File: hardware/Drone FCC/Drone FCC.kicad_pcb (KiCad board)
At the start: 4 copper layers, 60 x 100 mm, 160 parts, among them J1 UARTs externo x 3, J1001 SPI externo, J1003 I2C externo x2, J1005 5V y 3V3 x 2, J201 Mag Dupont, J202 Mag DF13, J203 GPS Dupont, J204 GPS M8N - DF13, J301 ESC 1, J302 ESC 2, J303 ESC 3, J304 ESC 4, J305 ESC 5, J306 ESC 6, J307 ESC 7, J308 ESC 8, J309 SERVO 1, J310 SERVO 2, J311 SERVO 3, J312 SERVO 4, J313 Power Servo, J401 DSM Spektrum JST, J402 PPM Dupont, J501 Micro USB - B, J601 SWD Debug Connector, J701 DM3AT-SF-PEJM5, J801 CAN 1 Connector 1, J803 CAN 2 Connector 1, J901 PM02 PixHawk, Q1101 2N7002, Q1102 2N7002, Q1103 2N7002, Q1104 2N7002, Q1105 2N7002, Q1106 2N7002, Q1107 2N7002, Q1108 2N7002, SW101 SW RESET, SW1101 SW Proposito General, SW1102 SW Proposito General, U101 STM32F746ZGTx, U201 ICM-42688-V, U202 HLGA_10L_STM, U501 USBLC6-2SC6, U801 SN65HVD230, U802 SN65HVD230, U901 ZLDO1117QG33TA, Y101 12MHz, Y102 32.768kHz

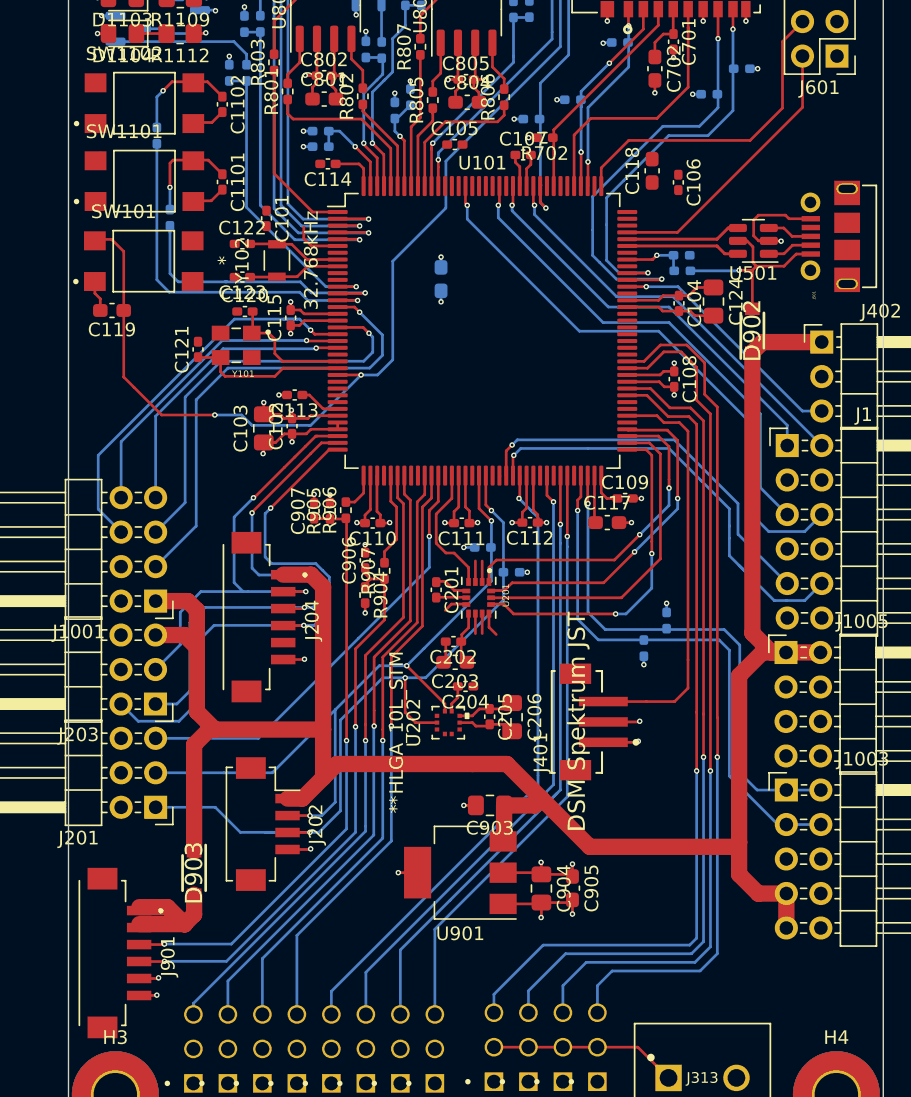
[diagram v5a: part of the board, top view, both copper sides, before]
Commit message: LDO layout on PCB
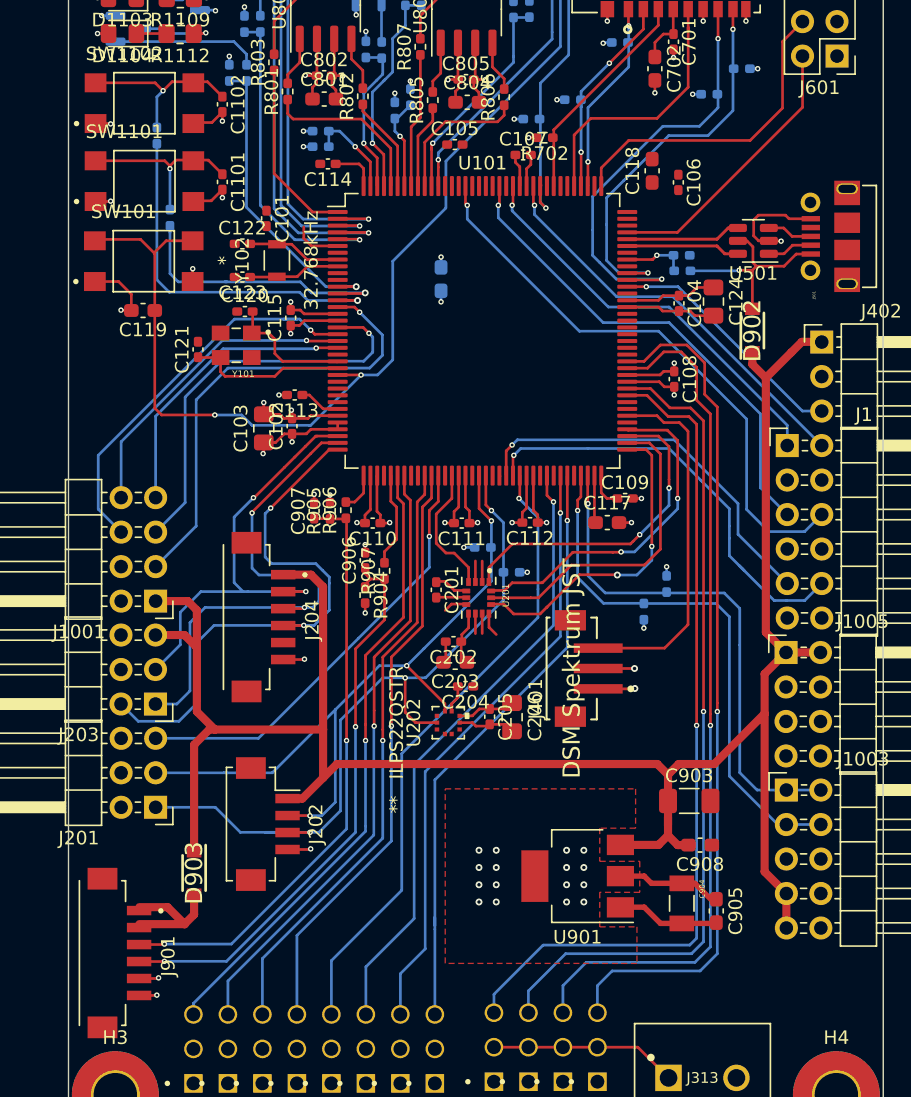
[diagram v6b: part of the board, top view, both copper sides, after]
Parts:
- added C908: 100n, Capacitor_SMD:C_0603_1608Metric_Pad1.08x0.95mm_HandSolder, F.Cu at (169.0, 123.8)
- C903: value 10u -> 4.7u; footprint Capacitor_SMD:C_0805_2012Metric_Pad1.18x1.45mm_HandSolder -> Capacitor_SMD:C_1206_3216Metric_Pad1.33x1.80mm_HandSolder
- C904: footprint Capacitor_SMD:C_0805_2012Metric_Pad1.18x1.45mm_HandSolder -> T491A106K016ATAUTO:CAPC3216X110N
- U202: value HLGA_10L_STM -> ILPS22QSTR
- moved C903 14.7 mm to (168.2, 120.6), turned to 0 degrees
- moved C905 10.7 mm to (170.2, 128.7)
- moved C904 10.4 mm to (167.7, 128.1)
- moved U901 8.64 mm to (160.0, 126.1)
- moved J401 3.96 mm to (159.6, 110.8)
- moved R106 2.69 mm to (164.9, 106.6)
- moved R105 2.69 mm to (166.6, 104.6)
- moved C119 2.29 mm to (128.0, 84.5)
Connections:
- J301 pad 2: /Motores_servos_PWM/Vdd_motors -> unconnected-(J301-Pad2)
- J302 pad 2: /Motores_servos_PWM/Vdd_motors -> unconnected-(J302-Pad2)
- J303 pad 2: /Motores_servos_PWM/Vdd_motors -> unconnected-(J303-Pad2)
- J304 pad 2: /Motores_servos_PWM/Vdd_motors -> unconnected-(J304-Pad2)
- J305 pad 2: /Motores_servos_PWM/Vdd_motors -> unconnected-(J305-Pad2)
- J306 pad 2: /Motores_servos_PWM/Vdd_motors -> unconnected-(J306-Pad2)
- J307 pad 2: /Motores_servos_PWM/Vdd_motors -> unconnected-(J307-Pad2)
- J308 pad 2: /Motores_servos_PWM/Vdd_motors -> unconnected-(J308-Pad2)
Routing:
- net GND: track 127.3 -> 133.7 mm, vias 56 -> 59
- net Net-(C1101-Pad1): track 8.99 -> 14.7 mm
- net Net-(C1102-Pad1): track 7.99 -> 13.2 mm
- net /Debug/NRST: track 93.0 -> 97.5 mm
- net /MCU/USART3_RX: track 30.5 -> 26.5 mm
- net 5V: track 150.0 -> 152.8 mm
- net /MCU/SPI2_CS: track 24.7 -> 23.5 mm
- net /MCU/TIM1_CH3: track 45.6 -> 44.6 mm
- net 3V3: track 104.9 -> 104.1 mm, vias 34 -> 47
- net /MCU/TIM1_CH4: track 43.7 -> 44.3 mm
- added copper zone on F.Cu, net 3V3

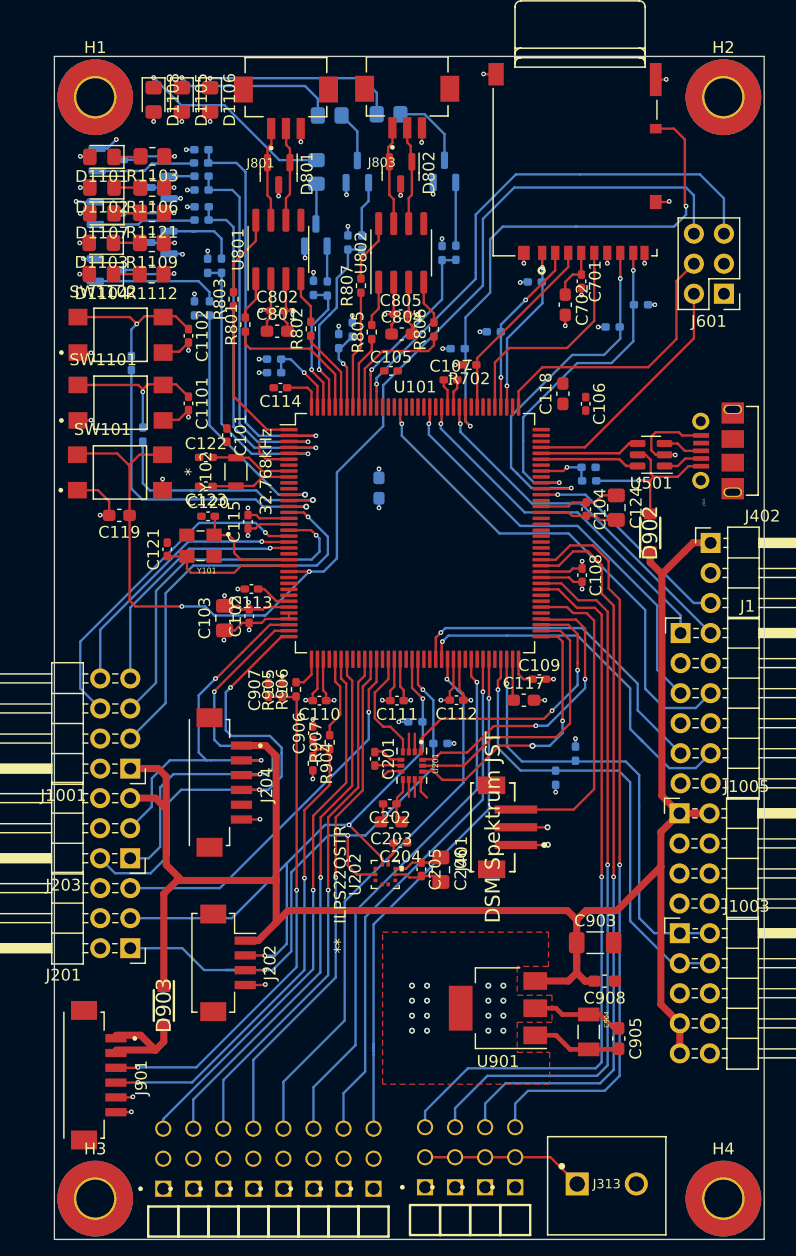
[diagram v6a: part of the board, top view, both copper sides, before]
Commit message: CAN PCB layout, positioned series resistors CAN TX and CAN RX
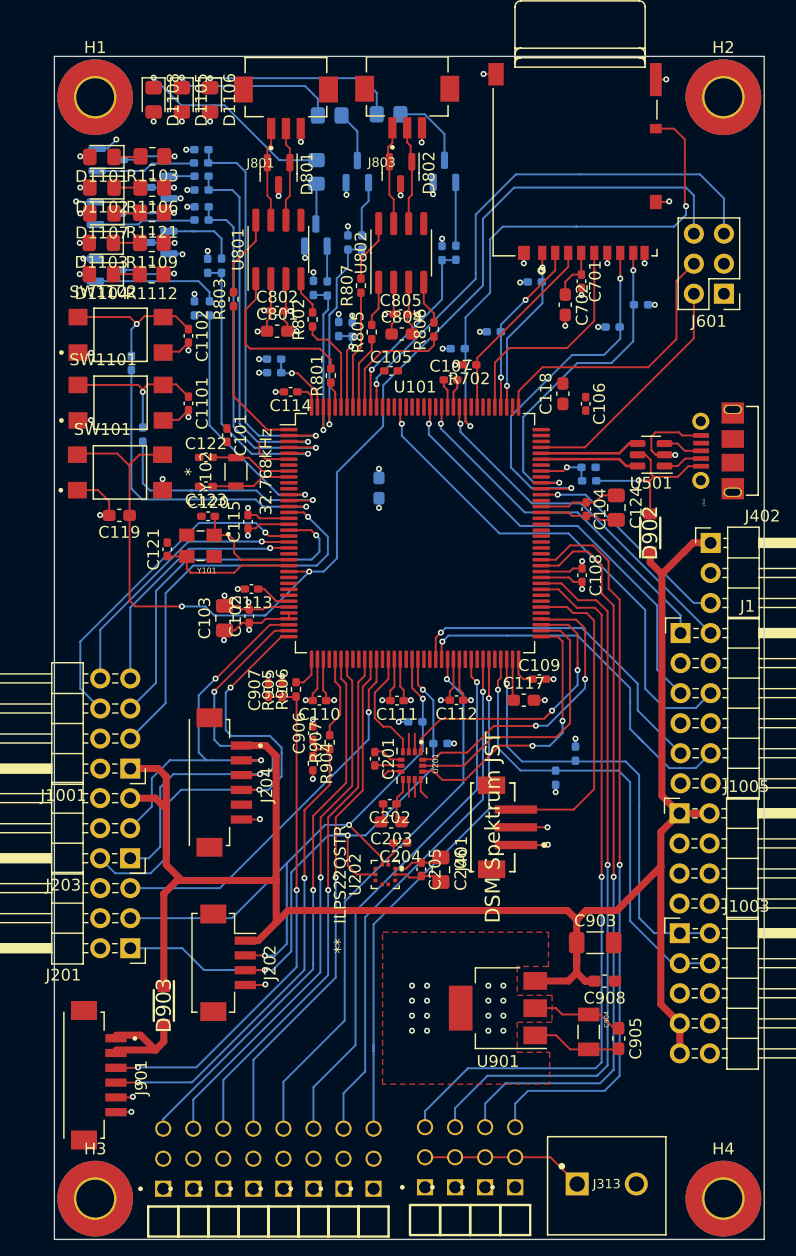
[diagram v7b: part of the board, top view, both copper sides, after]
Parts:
- R801: value 220 -> 50
- R802: value 220 -> 510
- moved R801 8.42 mm to (145.9, 72.6)
- moved R108 1.02 mm to (146.6, 68.7)
- moved C114 0.93 mm to (142.5, 74.0)
- moved R802 0.80 mm to (144.3, 67.9)
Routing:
- net Net-(R801-Pad2): track 3.65 -> 14.4 mm
- net /Interfaz_CAN/CAN1_TX: track 12.5 -> 2.40 mm
- net /Leds indicadores + pulsadores/LED8: track 11.6 -> 14.7 mm
- net /Leds indicadores + pulsadores/LED5: track 15.9 -> 18.4 mm
- net /Interfaz_CAN/CAN1_RX: track 7.07 -> 8.29 mm
- net GND: track 133.7 -> 134.9 mm, vias 59 -> 61
- net /MCU/PDR_ON: track 6.93 -> 6.11 mm
- net Net-(R802-Pad2): track 3.98 -> 3.25 mm
- net 3V3: track 104.1 -> 103.4 mm, vias 47 -> 48

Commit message: fix: moved series resistors from CANTX2 and CANRX2
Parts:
- moved R805 3.73 mm to (148.5, 72.6)
- moved C105 0.78 mm to (151.2, 73.0)
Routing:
- net /Debug/SWO: track 45.9 -> 31.7 mm, vias 1 -> 0
- net /Leds indicadores + pulsadores/LED6: track 16.1 -> 4.49 mm, vias 1 -> 0
- net Net-(R805-Pad2): track 3.86 -> 7.84 mm
- net /Interfaz_CAN/CAN2_TX: track 6.19 -> 2.20 mm
- net GND: track 134.9 -> 138.2 mm, vias 61 -> 62
- net 3V3: track 103.4 -> 106.6 mm, vias 48 -> 49
